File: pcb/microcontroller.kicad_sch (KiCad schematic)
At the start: 11 parts, among them J1 TagConnect_TC2030, SW1 TS-1187A-B-A-B, SW2 TS-1187A-B-A-B, U2 ESP32-S3-MINI-1-N8, U3 AMS1117-3.3

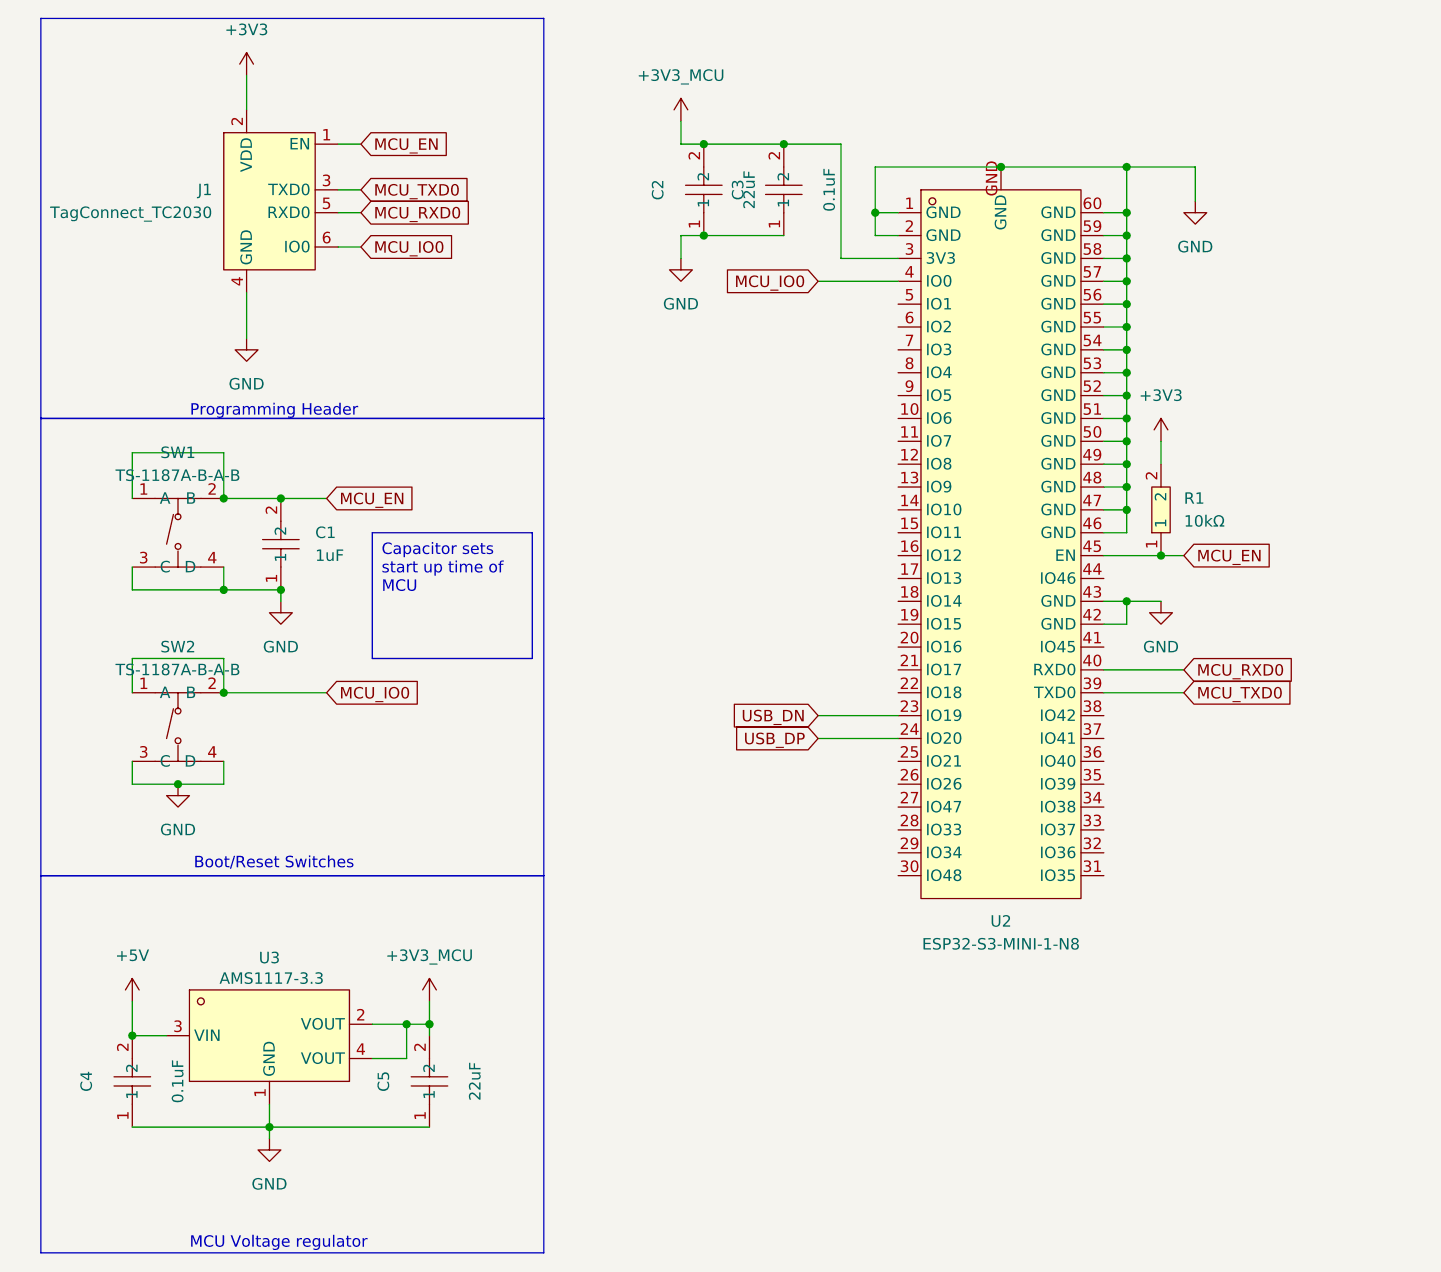
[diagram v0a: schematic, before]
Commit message: Starting on the SMPS
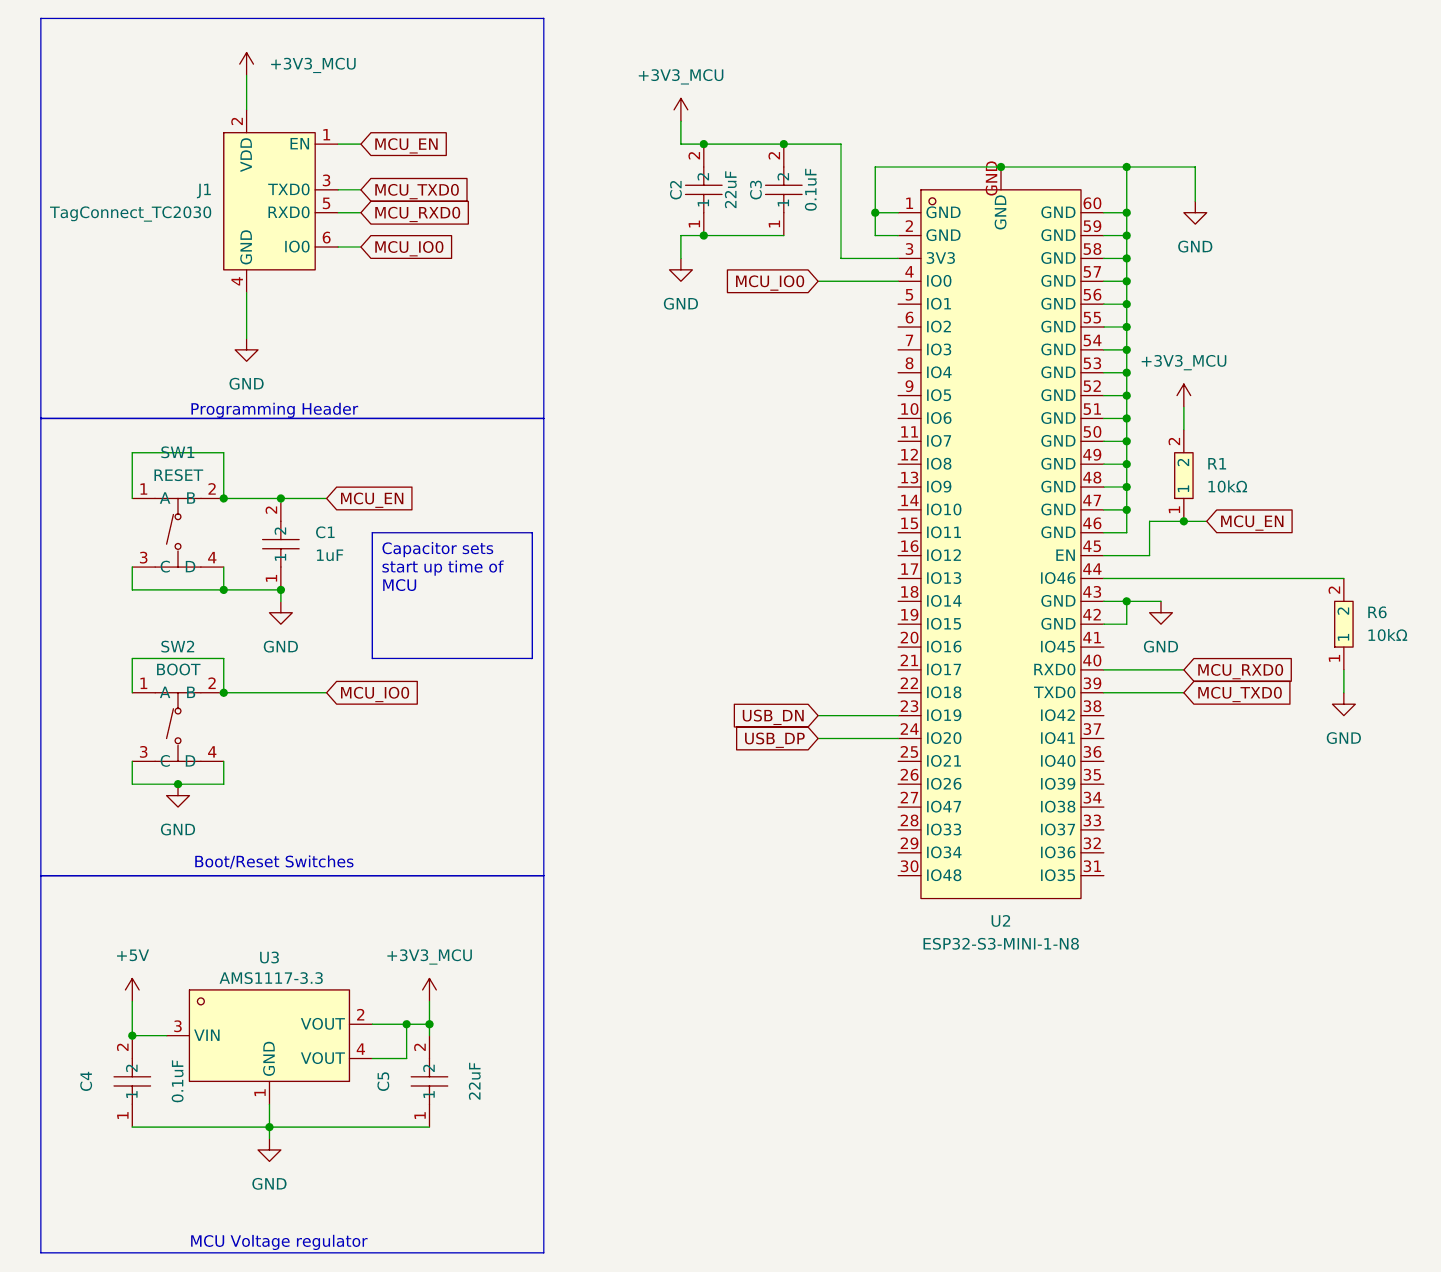
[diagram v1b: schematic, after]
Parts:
- added R6: 10kΩ, EasyEDA:R0603, symbol EasyEDA:10kΩ 0603
- SW1: value TS-1187A-B-A-B -> RESET
- SW2: value TS-1187A-B-A-B -> BOOT
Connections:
- net +3V3 is gone; now on net +3V3_MCU: J1.2 (VDD), R1.2
- net GND: now also R6.1
- net at U2.44 (IO46): now also R6.2
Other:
- moved on the sheet: R1
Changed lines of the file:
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@@
 	)
 	(junction
-		(at 137.16 72.39)
+		(at 139.7 68.58)
 		(diameter 0)
 		(color 0 0 0 0)
@@
 	(wire
 		(pts
-			(xy 137.16 72.39) (xy 139.7 72.39)
+			(xy 139.7 68.58) (xy 142.24 68.58)
 		)
 		(stroke
@@
 	(wire
 		(pts
+			(xy 135.89 68.58) (xy 135.89 72.39)
+		)
+		(stroke
+			(width 0)
+			(type default)
+		)
+	)
+	(wire
+		(pts
 			(xy 105.41 29.21) (xy 119.38 29.21)
 		)
@@
 	(wire
 		(pts
+			(xy 135.89 72.39) (xy 130.81 72.39)
+		)
+		(stroke
+			(width 0)
+			(type default)
+		)
+	)
+	(wire
+		(pts
 			(xy 99.06 41.91) (xy 107.95 41.91)
 		)
@@
 	(wire
 		(pts
+			(xy 157.48 85.09) (xy 157.48 87.63)
+		)
+		(stroke
+			(width 0)
+			(type default)
+		)
+	)
+	(wire
+		(pts
 			(xy 55.88 124.46) (xy 55.88 125.73)
 		)
@@
 	(wire
 		(pts
+			(xy 130.81 74.93) (xy 157.48 74.93)
+		)
+		(stroke
+			(width 0)
+			(type default)
+		)
+	)
+	(wire
+		(pts
 			(xy 22.86 135.89) (xy 38.1 135.89)
 		)
@@
 	(wire
 		(pts
-			(xy 137.16 59.69) (xy 137.16 62.23)
+			(xy 139.7 55.88) (xy 139.7 58.42)
 		)
 		(stroke
@@
 	(wire
 		(pts
-			(xy 130.81 72.39) (xy 137.16 72.39)
-		)
-		(stroke
-			(width 0)
-			(type default)
-		)
-	)
-	(wire
-		(pts
 			(xy 39.37 66.04) (xy 44.45 66.04)
 		)
@@
 		(pts
 			(xy 133.35 49.53) (xy 133.35 46.99)
+		)
+		(stroke
+			(width 0)
+			(type default)
+		)
+	)
+	(wire
+		(pts
+			(xy 135.89 68.58) (xy 139.7 68.58)
 		)
 		(stroke
@@
 	(global_label "MCU_EN"
 		(shape input)
-		(at 139.7 72.39 0)
+		(at 142.24 68.58 0)
 		(fields_autoplaced yes)
 		(effects
@@
 		)
 		(property "Intersheetrefs" "${INTERSHEET_REFS}"
-			(at 150.1842 72.39 0)
+			(at 152.7242 68.58 0)
 			(effects
 				(font
@@
 				(justify left)
 				(hide yes)
+			)
+		)
+	)
+	(symbol
+		(lib_id "EasyEDA:10kΩ 0603")
+		(at 157.48 80.01 90)
+		(unit 1)
+		(exclude_from_sim no)
+		(in_bom yes)
+		(on_board yes)
+		(dnp no)
+		(fields_autoplaced yes)
+		(property "Reference" "R6"
+			(at 160.02 78.7399 90)
+			(effects
+				(font
+					(size 1.27 1.27)
+				)
+				(justify right)
+			)
+		)
+		(property "Value" "10kΩ"
+			(at 160.02 81.2799 90)
+			(effects
+				(font
+					(size 1.27 1.27)
+				)
+				(justify right)
+			)
+		)
+		(property "Footprint" "EasyEDA:R0603"
+			(at 165.1 80.01 0)
+			(effects
+				(font
+					(size 1.27 1.27)
+				)
+				(hide yes)
+			)
+		)
+		(property "Datasheet" "https://lcsc.com/product-detail/Chip-Resistor-Surface-Mount-UniOhm_10KR-1002-1_C25804.html"
+			(at 167.64 80.01 0)
+			(effects
+				(font
+					(size 1.27 1.27)
+				)
+				(hide yes)
+			)
+		)
+		(property "Description" "0603WAF1002T5E"
+			(at 157.48 80.01 0)
+			(effects
+				(font
+					(size 1.27 1.27)
+				)
+				(hide yes)
+			)
+		)
+		(property "LCSC Part" "C25804"
+			(at 170.18 80.01 0)
+			(effects
+				(font
+					(size 1.27 1.27)
+				)
+				(hide yes)
+			)
+		)
+		(pin "2"
+		)
+		(pin "1"
+		)
+		(instances
+			(project "pcb"
+				(path "/7efcc018-2ceb-4b85-a682-18e44d24826b/77e24cbc-bef9-40f4-87d1-6c1611733373"
+					(reference "R6")
+					(unit 1)
+				)
 			)
 		)
@@
 			)
 		)
-		(property "Value" "TS-1187A-B-A-B"
+		(property "Value" "RESET"
 			(at 27.94 63.5 0)
 			(effects
@@
 		(dnp no)
 		(property "Reference" "C3"
-			(at 90.17 31.75 0)
+			(at 92.202 31.75 0)
 			(effects
 				(font
@@
 		)
 		(property "Value" "0.1uF"
-			(at 100.33 31.75 0)
+			(at 98.298 31.75 0)
 			(effects
 				(font
@@
 	(symbol
 		(lib_id "power:+3V3")
-		(at 137.16 59.69 0)
+		(at 139.7 55.88 0)
 		(unit 1)
 		(exclude_from_sim no)
@@
 		(fields_autoplaced yes)
 		(property "Reference" "#PWR05"
-			(at 137.16 63.5 0)
-			(effects
-				(font
-					(size 1.27 1.27)
-				)
-				(hide yes)
-			)
-		)
-		(property "Value" "+3V3"
-			(at 137.16 54.61 0)
+			(at 139.7 59.69 0)
+			(effects
+				(font
+					(size 1.27 1.27)
+				)
+				(hide yes)
+			)
+		)
+		(property "Value" "+3V3_MCU"
+			(at 139.7 50.8 0)
 			(effects
 				(font
@@
 		)
 		(property "Footprint" ""
-			(at 137.16 59.69 0)
+			(at 139.7 55.88 0)
 			(effects
 				(font
@@
 		)
 		(property "Datasheet" ""
-			(at 137.16 59.69 0)
+			(at 139.7 55.88 0)
 			(effects
 				(font
@@
 		)
 		(property "Description" "Power symbol creates a global label with name \"+3V3\""
-			(at 137.16 59.69 0)
+			(at 139.7 55.88 0)
 			(effects
 				(font
@@
 			)
 		)
-		(property "Value" "+3V3"
-			(at 35.56 13.97 0)
-			(effects
-				(font
-					(size 1.27 1.27)
-				)
+		(property "Value" "+3V3_MCU"
+			(at 38.1 17.7799 0)
+			(effects
+				(font
+					(size 1.27 1.27)
+				)
+				(justify left)
 			)
 		)
@@
 				(path "/7efcc018-2ceb-4b85-a682-18e44d24826b/77e24cbc-bef9-40f4-87d1-6c1611733373"
 					(reference "#PWR08")
+					(unit 1)
+				)
+			)
+		)
+	)
+	(symbol
+		(lib_id "power:GND")
+		(at 157.48 87.63 0)
+		(unit 1)
+		(exclude_from_sim no)
+		(in_bom yes)
+		(on_board yes)
+		(dnp no)
+		(fields_autoplaced yes)
+		(property "Reference" "#PWR025"
+			(at 157.48 93.98 0)
+			(effects
+				(font
+					(size 1.27 1.27)
+				)
+				(hide yes)
+			)
+		)
+		(property "Value" "GND"
+			(at 157.48 92.71 0)
+			(effects
+				(font
+					(size 1.27 1.27)
+				)
+			)
+		)
+		(property "Footprint" ""
+			(at 157.48 87.63 0)
+			(effects
+				(font
+					(size 1.27 1.27)
+				)
+				(hide yes)
+			)
+		)
+		(property "Datasheet" ""
+			(at 157.48 87.63 0)
+			(effects
+				(font
+					(size 1.27 1.27)
+				)
+				(hide yes)
+			)
+		)
+		(property "Description" "Power symbol creates a global label with name \"GND\" , ground"
+			(at 157.48 87.63 0)
+			(effects
+				(font
+					(size 1.27 1.27)
+				)
+				(hide yes)
+			)
+		)
+		(pin "1"
+		)
+		(instances
+			(project "pcb"
+				(path "/7efcc018-2ceb-4b85-a682-18e44d24826b/77e24cbc-bef9-40f4-87d1-6c1611733373"
+					(reference "#PWR025")
 					(unit 1)
 				)
@@
 		(dnp no)
 		(property "Reference" "C2"
-			(at 81.28 31.75 0)
+			(at 83.312 31.75 0)
 			(effects
 				(font
@@
 		)
 		(property "Value" "22uF"
-			(at 91.44 31.75 0)
+			(at 89.408 31.75 0)
 			(effects
 				(font
@@
 			)
 		)
-		(property "Value" "TS-1187A-B-A-B"
+		(property "Value" "BOOT"
 			(at 27.94 85.09 0)
 			(effects
@@
 	(symbol
 		(lib_id "EasyEDA:10kΩ 0603")
-		(at 137.16 67.31 90)
+		(at 139.7 63.5 90)
 		(unit 1)
 		(exclude_from_sim no)
@@
 		(fields_autoplaced yes)
 		(property "Reference" "R1"
-			(at 139.7 66.0399 90)
+			(at 142.24 62.2299 90)
 			(effects
 				(font
@@
 		)
 		(property "Value" "10kΩ"
-			(at 139.7 68.5799 90)
+			(at 142.24 64.7699 90)
 			(effects
 				(font
@@
 		)
 		(property "Footprint" "EasyEDA:R0603"
-			(at 144.78 67.31 0)
+			(at 147.32 63.5 0)
 			(effects
 				(font
@@
 		)
 		(property "Datasheet" "https://lcsc.com/product-detail/Chip-Resistor-Surface-Mount-UniOhm_10KR-1002-1_C25804.html"
-			(at 147.32 67.31 0)
+			(at 149.86 63.5 0)
 			(effects
 				(font
@@
 		)
 		(property "Description" "0603WAF1002T5E"
-			(at 137.16 67.31 0)
+			(at 139.7 63.5 0)
 			(effects
 				(font
@@
 		)
 		(property "LCSC Part" "C25804"
-			(at 149.86 67.31 0)
-			(effects
-				(font
+			(at 152.4 63.5 0)
+			(effects
+				(font
